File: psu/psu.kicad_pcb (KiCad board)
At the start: 2 copper layers, 101.6 x 68.6 mm, 21 parts, among them J1 Conn_01x02_Socket, J2 Conn_01x03_Socket, U1 L7812, U2 L7912

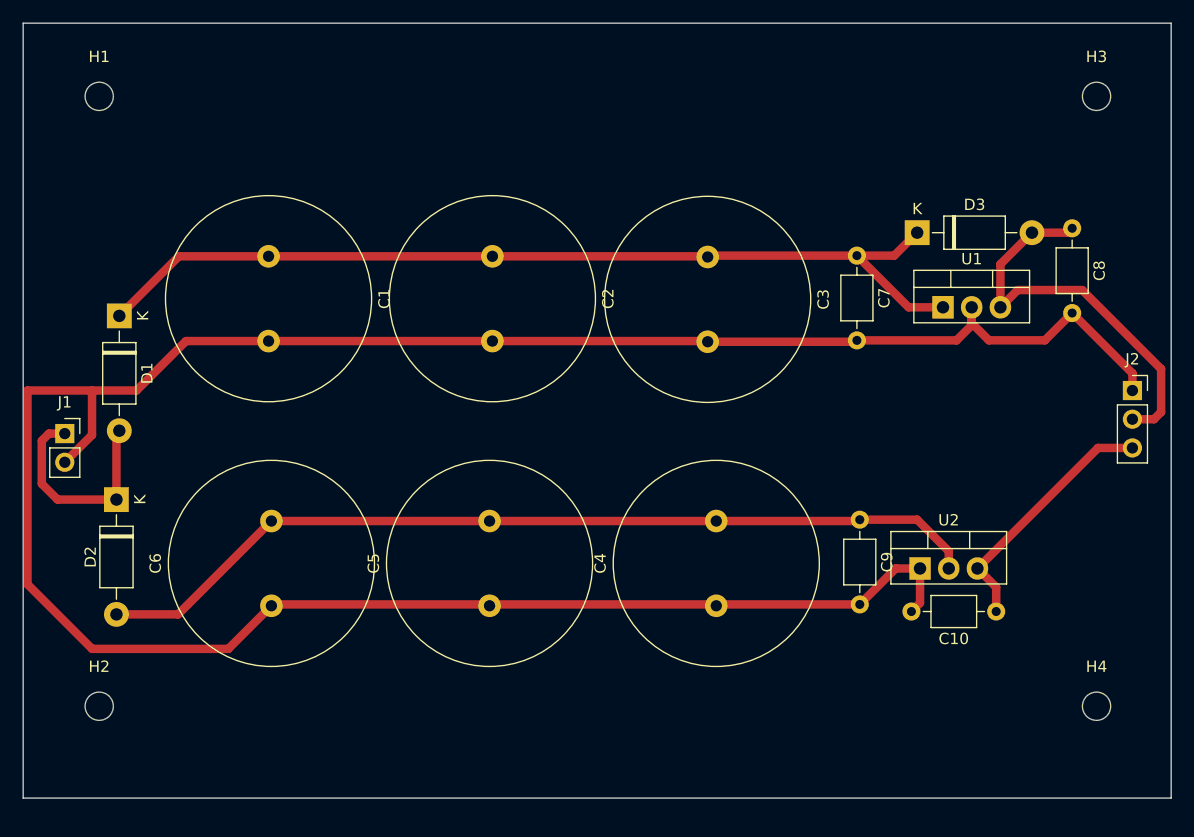
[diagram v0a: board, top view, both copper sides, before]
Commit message: add psu bom, improve trace width
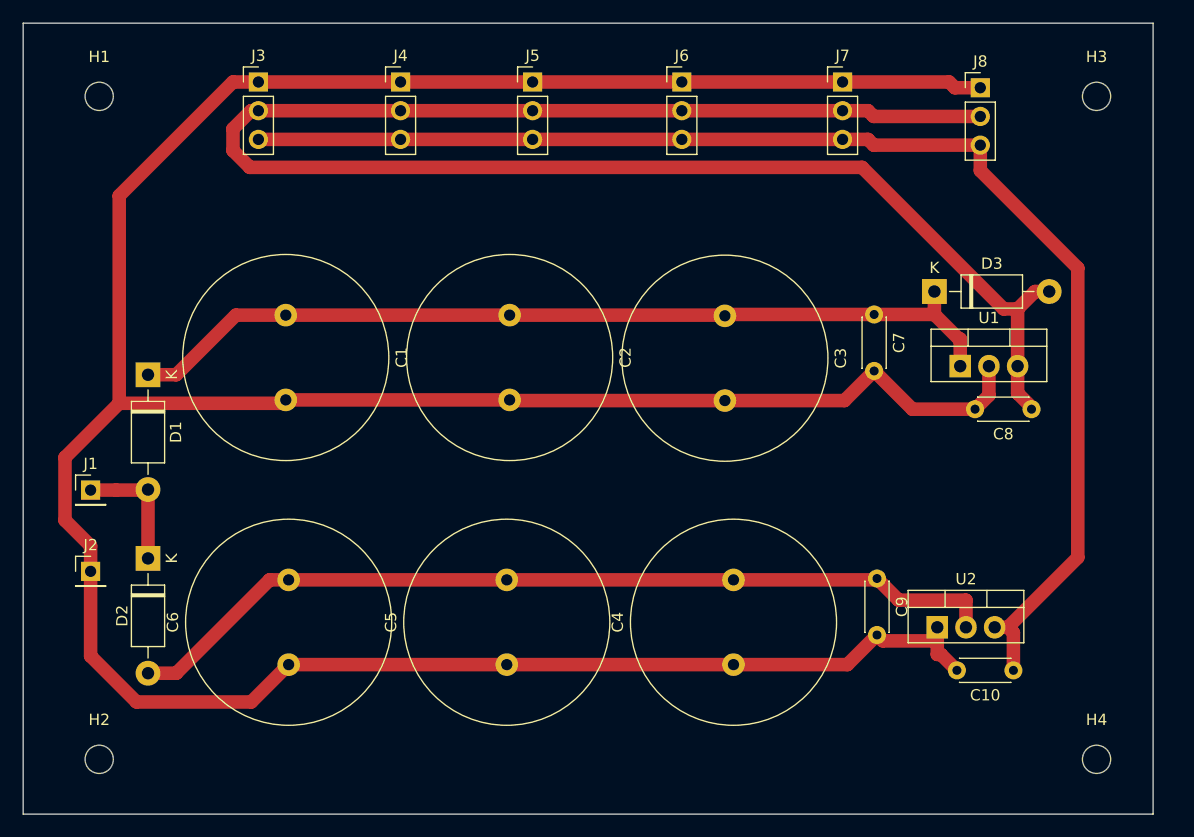
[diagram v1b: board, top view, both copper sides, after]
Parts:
- added J3: Conn_01x03_Pin, Connector_PinHeader_2.54mm:PinHeader_1x03_P2.54mm_Vertical, F.Cu at (33.1, 17.8)
- added J4: Conn_01x03_Pin, Connector_PinHeader_2.54mm:PinHeader_1x03_P2.54mm_Vertical, F.Cu at (45.7, 17.8)
- added J5: Conn_01x03_Pin, Connector_PinHeader_2.54mm:PinHeader_1x03_P2.54mm_Vertical, F.Cu at (57.4, 17.8)
- added J6: Conn_01x03_Pin, Connector_PinHeader_2.54mm:PinHeader_1x03_P2.54mm_Vertical, F.Cu at (70.6, 17.8)
- added J7: Conn_01x03_Pin, Connector_PinHeader_2.54mm:PinHeader_1x03_P2.54mm_Vertical, F.Cu at (84.8, 17.8)
- added J8: Conn_01x03_Pin, Connector_PinHeader_2.54mm:PinHeader_1x03_P2.54mm_Vertical, F.Cu at (97.0, 18.3)
- C1, C2, C3, C4, C5, C6: value C_Polarized -> 4700u
- C10, C7, C8, C9: value C -> 1u; footprint Capacitor_THT:C_Axial_L3.8mm_D2.6mm_P7.50mm_Horizontal -> Capacitor_THT:C_Disc_D4.3mm_W1.9mm_P5.00mm
- J1: value Conn_01x02_Socket -> Conn_01x01_Pin; footprint Connector_PinSocket_2.54mm:PinSocket_1x02_P2.54mm_Vertical -> Connector_PinHeader_2.54mm:PinHeader_1x01_P2.54mm_Vertical
- J2: value Conn_01x03_Socket -> Conn_01x01_Pin; footprint Connector_PinSocket_2.54mm:PinSocket_1x03_P2.54mm_Vertical -> Connector_PinHeader_2.54mm:PinHeader_1x01_P2.54mm_Vertical
- moved J2 93.6 mm to (18.3, 61.1)
- moved C8 16.4 mm to (101.6, 46.7), turned to 180 degrees
- moved D2 5.91 mm to (23.4, 59.9)
- moved D1 5.79 mm to (23.4, 43.7)
- moved J1 5.50 mm to (18.3, 53.9)
- moved U2 5.43 mm to (93.2, 66.0)
- moved D3 5.43 mm to (93.0, 36.3)
- moved C1 5.43 mm to (35.6, 38.4)
- moved C2 5.43 mm to (55.4, 38.4)
- moved C7 5.43 mm to (87.6, 38.4)
- moved C9 5.43 mm to (87.9, 61.7)
- moved U1 5.43 mm to (95.2, 42.9)
- moved C10 5.43 mm to (100.0, 69.8)
- moved C3 5.43 mm to (74.4, 38.5)
- moved C4 5.43 mm to (75.2, 69.3)
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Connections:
- C10 pad 1: Net-(J2-Pin_3) -> Net-(J3-Pin_3)
- U2 pad 3: Net-(J2-Pin_3) -> Net-(J3-Pin_3)
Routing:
- net Net-(D3-A): track 35.8 -> 157.0 mm
- net Net-(J3-Pin_3): track 0.00 -> 118.1 mm
- net GND: track 221.5 -> 291.0 mm
- net Net-(J2-Pin_3): track 22.6 -> 0.00 mm
- net +12VA: track 19.5 -> 11.2 mm
- net Net-(D1-K): track 83.2 -> 79.5 mm
- net Net-(D2-A): track 79.8 -> 79.1 mm
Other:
- board size 101.6 x 68.6 mm -> 100 x 70 mm
